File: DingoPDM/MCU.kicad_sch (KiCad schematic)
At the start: 25 parts, among them J4 TC, SW1 BOOT, U3 PCA82C250, U4 STM32F446RETx, Y1 8mHz

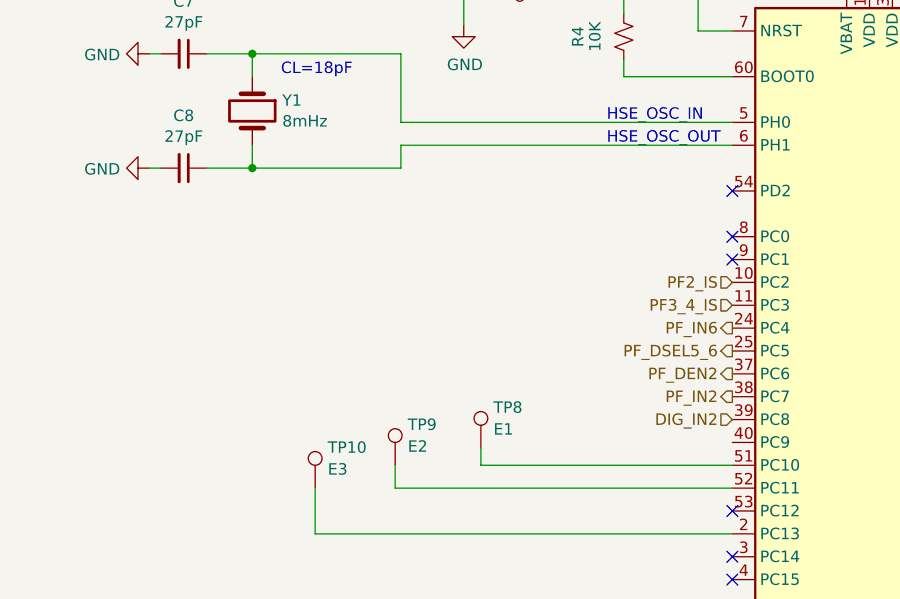
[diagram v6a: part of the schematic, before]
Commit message: V7.1 Fixes
SDA/SCL mixed up on FRAM, added status LEDs, switched to thermal relief zones
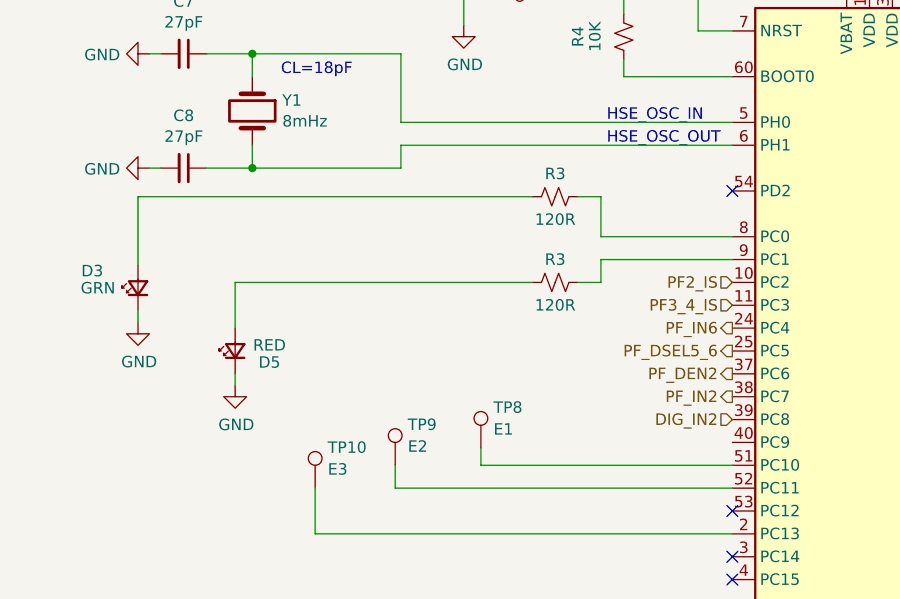
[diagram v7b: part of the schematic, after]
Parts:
- added D3: GRN, LED_SMD:LED_0805_2012Metric, symbol Device:LED_Small
- added D5: RED, LED_SMD:LED_0805_2012Metric, symbol Device:LED_Small
- added R3 (x2): 120R, Resistor_SMD:R_0805_2012Metric, symbol Device:R_Small_US
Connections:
- net GND: now also D3.1 (K), D5.1 (K)
- net at U4.8 (PC0): now also R3.1
- net at U4.9 (PC1): now also R3.1
- new net: D3.2 (A), R3.2
- new net: D5.2 (A), R3.2
- no-connect marks 9 -> 7
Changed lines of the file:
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@@
   (title_block
     (title "Dingo_PDM")
-    (date "2023-07-28")
-    (rev "v6")
+    (date "2023-09-04")
+    (rev "v7.1")
     (comment 3 "github.com/corygrant")
     (comment 4 "Cory Grant")
@@
   (junction (at 114.3 23.495) (diameter 0) (color 0 0 0 0)
   )
-  (no_connect (at 91.44 62.865))
   (no_connect (at 91.44 90.805))
   (no_connect (at 127 75.565))
   (no_connect (at 91.44 95.885))
   (no_connect (at 127 93.345))
-  (no_connect (at 91.44 60.325))
   (no_connect (at 127 90.805))
   (no_connect (at 91.44 98.425))
@@
     (stroke (width 0) (type default))
   )
+  (wire (pts (xy 69.215 55.88) (xy 25.4 55.88))
+    (stroke (width 0) (type default))
+  )
   (wire (pts (xy 114.3 23.495) (xy 114.3 32.385))
     (stroke (width 0) (type default))
@@
     (stroke (width 0) (type default))
   )
+  (wire (pts (xy 36.195 76.835) (xy 36.195 75.565))
+    (stroke (width 0) (type default))
+  )
   (wire (pts (xy 116.84 29.845) (xy 116.84 32.385))
     (stroke (width 0) (type default))
@@
     (stroke (width 0) (type default))
   )
+  (wire (pts (xy 76.835 60.325) (xy 76.835 55.88))
+    (stroke (width 0) (type default))
+  )
   (wire (pts (xy 79.375 167.64) (xy 85.725 167.64))
     (stroke (width 0) (type default))
@@
     (stroke (width 0) (type default))
   )
+  (wire (pts (xy 76.835 65.405) (xy 74.295 65.405))
+    (stroke (width 0) (type default))
+  )
+  (wire (pts (xy 76.835 62.865) (xy 76.835 65.405))
+    (stroke (width 0) (type default))
+  )
   (wire (pts (xy 98.425 184.15) (xy 98.425 180.34))
     (stroke (width 0) (type default))
@@
     (stroke (width 0) (type default))
   )
+  (wire (pts (xy 76.835 55.88) (xy 74.295 55.88))
+    (stroke (width 0) (type default))
+  )
   (wire (pts (xy 38.1 40.005) (xy 33.02 40.005))
     (stroke (width 0) (type default))
@@
     (stroke (width 0) (type default))
   )
+  (wire (pts (xy 25.4 55.88) (xy 25.4 63.5))
+    (stroke (width 0) (type default))
+  )
   (wire (pts (xy 63.5 85.725) (xy 63.5 83.82))
     (stroke (width 0) (type default))
@@
     (stroke (width 0) (type default))
   )
+  (wire (pts (xy 91.44 60.325) (xy 76.835 60.325))
+    (stroke (width 0) (type default))
+  )
   (wire (pts (xy 109.22 23.495) (xy 111.76 23.495))
     (stroke (width 0) (type default))
@@
     (stroke (width 0) (type default))
   )
+  (wire (pts (xy 25.4 69.85) (xy 25.4 68.58))
+    (stroke (width 0) (type default))
+  )
+  (wire (pts (xy 91.44 62.865) (xy 76.835 62.865))
+    (stroke (width 0) (type default))
+  )
   (wire (pts (xy 26.67 52.705) (xy 27.94 52.705))
     (stroke (width 0) (type default))
@@
     (stroke (width 0) (type default))
   )
+  (wire (pts (xy 69.215 65.405) (xy 36.195 65.405))
+    (stroke (width 0) (type default))
+  )
   (wire (pts (xy 38.1 50.165) (xy 38.1 52.705))
     (stroke (width 0) (type default))
@@
   )
   (wire (pts (xy 127 88.265) (xy 138.43 88.265))
+    (stroke (width 0) (type default))
+  )
+  (wire (pts (xy 36.195 65.405) (xy 36.195 70.485))
     (stroke (width 0) (type default))
   )
@@
     )
   )
+  (symbol (lib_id "Device:LED_Small") (at 25.4 66.04 90) (unit 1)
+    (in_bom yes) (on_board yes) (dnp no)
+    (property "Reference" "D3" (at 20.32 64.135 90)
+      (effects (font (size 1.27 1.27)))
+    )
+    (property "Value" "GRN" (at 20.955 66.04 90)
+      (effects (font (size 1.27 1.27)))
+    )
+    (property "Footprint" "LED_SMD:LED_0805_2012Metric" (at 25.4 66.04 90)
+      (effects (font (size 1.27 1.27)) hide)
+    )
+    (property "Datasheet" "" (at 25.4 66.04 90)
+      (effects (font (size 1.27 1.27)) hide)
+    )
+    (property "Digi-Key_PN" "475-1410-1-ND" (at 25.4 66.04 0)
+      (effects (font (size 1.27 1.27)) hide)
+    )
+    (property "LCSC" "C2899888" (at 25.4 66.04 0)
+      (effects (font (size 1.27 1.27)) hide)
+    )
+    (pin "1")
+    (pin "2")
+    (instances
+      (project "DingoPDM"
+        (path "/8948e307-9174-4227-9c28-3ff885e6e83d/00000000-0000-0000-0000-00005f5cf2eb"
+          (reference "D3") (unit 1)
+        )
+        (path "/8948e307-9174-4227-9c28-3ff885e6e83d/00000000-0000-0000-0000-00005f4db108"
+          (reference "D16") (unit 1)
+        )
+      )
+    )
+  )
   (symbol (lib_id "Connector:TestPoint") (at 64.135 151.13 180) (unit 1)
     (in_bom yes) (on_board yes) (dnp no)
@@
         (path "/8948e307-9174-4227-9c28-3ff885e6e83d/00000000-0000-0000-0000-00005f4db108"
           (reference "TP2") (unit 1)
+        )
+      )
+    )
+  )
+  (symbol (lib_id "power:GND") (at 36.195 76.835 0) (unit 1)
+    (in_bom yes) (on_board yes) (dnp no)
+    (property "Reference" "#PWR016" (at 36.195 83.185 0)
+      (effects (font (size 1.27 1.27)) hide)
+    )
+    (property "Value" "GND" (at 36.322 81.2292 0)
+      (effects (font (size 1.27 1.27)))
+    )
+    (property "Footprint" "" (at 36.195 76.835 0)
+      (effects (font (size 1.27 1.27)) hide)
+    )
+    (property "Datasheet" "" (at 36.195 76.835 0)
+      (effects (font (size 1.27 1.27)) hide)
+    )
+    (pin "1")
+    (instances
+      (project "DingoPDM"
+        (path "/8948e307-9174-4227-9c28-3ff885e6e83d/00000000-0000-0000-0000-00005f5cf2eb"
+          (reference "#PWR016") (unit 1)
+        )
+        (path "/8948e307-9174-4227-9c28-3ff885e6e83d/00000000-0000-0000-0000-00005f4db108"
+          (reference "#PWR091") (unit 1)
         )
       )
@@
     )
   )
+  (symbol (lib_id "Device:R_Small_US") (at 71.755 65.405 270) (unit 1)
+    (in_bom yes) (on_board yes) (dnp no)
+    (property "Reference" "R3" (at 71.755 62.865 90)
+      (effects (font (size 1.27 1.27)))
+    )
+    (property "Value" "120R" (at 71.755 67.945 90)
+      (effects (font (size 1.27 1.27)))
+    )
+    (property "Footprint" "Resistor_SMD:R_0805_2012Metric" (at 71.755 65.405 0)
+      (effects (font (size 1.27 1.27)) hide)
+    )
+    (property "Datasheet" "" (at 71.755 65.405 0)
+      (effects (font (size 1.27 1.27)) hide)
+    )
+    (property "Digi-Key_PN" "311-120CRCT-ND" (at 71.755 65.405 0)
+      (effects (font (size 1.27 1.27)) hide)
+    )
+    (property "LCSC" "C229076" (at 71.755 65.405 0)
+      (effects (font (size 1.27 1.27)) hide)
+    )
+    (pin "1")
+    (pin "2")
+    (instances
+      (project "DingoPDM"
+        (path "/8948e307-9174-4227-9c28-3ff885e6e83d/00000000-0000-0000-0000-00005f5cf2eb"
+          (reference "R3") (unit 1)
+        )
+        (path "/8948e307-9174-4227-9c28-3ff885e6e83d/00000000-0000-0000-0000-00005f4db108"
+          (reference "R53") (unit 1)
+        )
+      )
+    )
+  )
   (symbol (lib_id "Connector:TestPoint") (at 45.085 88.265 0) (unit 1)
     (in_bom yes) (on_board yes) (dnp no) (fields_autoplaced)
@@
     )
   )
+  (symbol (lib_id "Device:LED_Small") (at 36.195 73.025 90) (unit 1)
+    (in_bom yes) (on_board yes) (dnp no)
+    (property "Reference" "D5" (at 40.005 74.295 90)
+      (effects (font (size 1.27 1.27)))
+    )
+    (property "Value" "RED" (at 40.005 72.39 90)
+      (effects (font (size 1.27 1.27)))
+    )
+    (property "Footprint" "LED_SMD:LED_0805_2012Metric" (at 36.195 73.025 90)
+      (effects (font (size 1.27 1.27)) hide)
+    )
+    (property "Datasheet" "" (at 36.195 73.025 90)
+      (effects (font (size 1.27 1.27)) hide)
+    )
+    (property "Digi-Key_PN" "475-1278-1-ND" (at 36.195 73.025 0)
+      (effects (font (size 1.27 1.27)) hide)
+    )
+    (property "LCSC" "C2899997" (at 36.195 73.025 0)
+      (effects (font (size 1.27 1.27)) hide)
+    )
+    (pin "1")
+    (pin "2")
+    (instances
+      (project "DingoPDM"
+        (path "/8948e307-9174-4227-9c28-3ff885e6e83d/00000000-0000-0000-0000-00005f5b7065"
+          (reference "D5") (unit 1)
+        )
+        (path "/8948e307-9174-4227-9c28-3ff885e6e83d/00000000-0000-0000-0000-00005f4db108"
+          (reference "D17") (unit 1)
+        )
+      )
+    )
+  )
+  (symbol (lib_id "power:GND") (at 25.4 69.85 0) (unit 1)
+    (in_bom yes) (on_board yes) (dnp no)
+    (property "Reference" "#PWR016" (at 25.4 76.2 0)
+      (effects (font (size 1.27 1.27)) hide)
+    )
+    (property "Value" "GND" (at 25.527 74.2442 0)
+      (effects (font (size 1.27 1.27)))
+    )
+    (property "Footprint" "" (at 25.4 69.85 0)
+      (effects (font (size 1.27 1.27)) hide)
+    )
+    (property "Datasheet" "" (at 25.4 69.85 0)
+      (effects (font (size 1.27 1.27)) hide)
+    )
+    (pin "1")
+    (instances
+      (project "DingoPDM"
+        (path "/8948e307-9174-4227-9c28-3ff885e6e83d/00000000-0000-0000-0000-00005f5cf2eb"
+          (reference "#PWR016") (unit 1)
+        )
+        (path "/8948e307-9174-4227-9c28-3ff885e6e83d/00000000-0000-0000-0000-00005f4db108"
+          (reference "#PWR090") (unit 1)
+        )
+      )
+    )
+  )
   (symbol (lib_id "Connector:TestPoint") (at 70.485 151.13 180) (unit 1)
     (in_bom yes) (on_board yes) (dnp no)
@@
         )
       )
+    )
+  )
+  (symbol (lib_id "Device:R_Small_US") (at 71.755 55.88 270) (unit 1)
+    (in_bom yes) (on_board yes) (dnp no)
+    (property "Reference" "R3" (at 71.755 53.34 90)
+      (effects (font (size 1.27 1.27)))
+    )
+    (property "Value" "120R" (at 71.755 58.42 90)
+      (effects (font (size 1.27 1.27)))
+    )
+    (property "Footprint" "Resistor_SMD:R_0805_2012Metric" (at 71.755 55.88 0)
+      (effects (font (size 1.27 1.27)) hide)
+    )
+    (property "Datasheet" "" (at 71.755 55.88 0)
+      (effects (font (size 1.27 1.27)) hide)
+    )
+    (property "Digi-Key_PN" "311-120CRCT-ND" (at 71.755 55.88 0)
+      (effects (font (size 1.27 1.27)) hide)
+    )
+    (property "LCSC" "C229076" (at 71.755 55.88 0)
+      (effects (font (size 1.27 1.27)) hide)
+    )
+    (pin "1")
+    (pin "2")
+    (instances
+      (project "DingoPDM"
+        (path "/8948e307-9174-4227-9c28-3ff885e6e83d/00000000-0000-0000-0000-00005f5cf2eb"
+          (reference "R3") (unit 1)
+        )
+        (path "/8948e307-9174-4227-9c28-3ff885e6e83d/00000000-0000-0000-0000-00005f4db108"
+          (reference "R52") (unit 1)
+        )
+      )

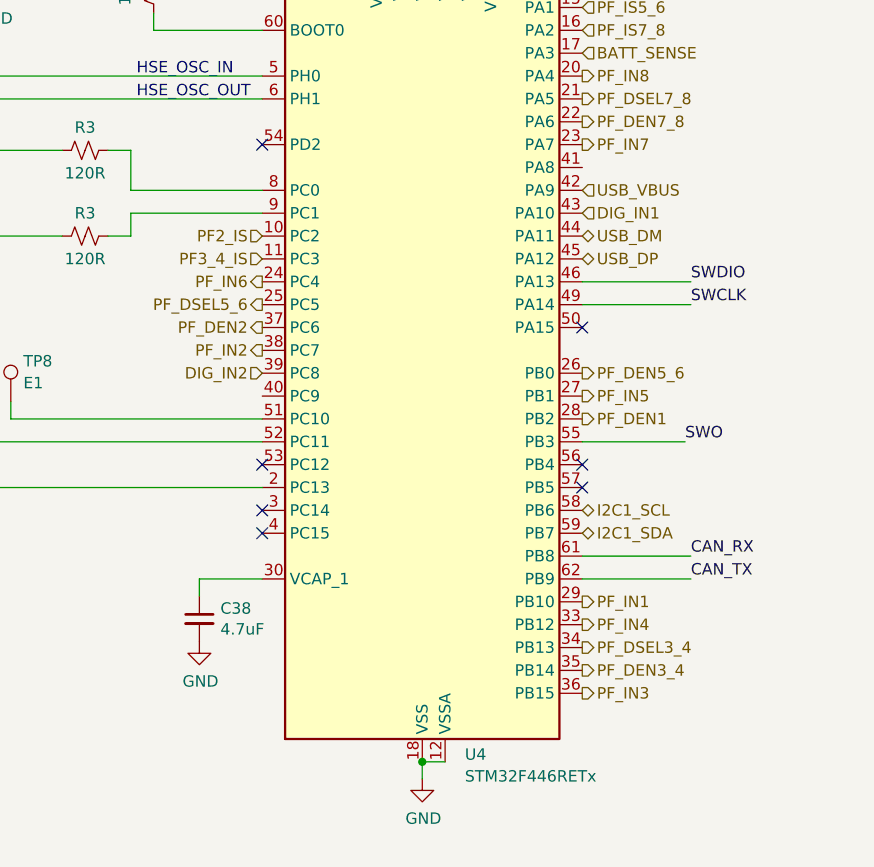
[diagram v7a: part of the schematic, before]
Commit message: Add diode, disconnect PB13, fix USB VBUS
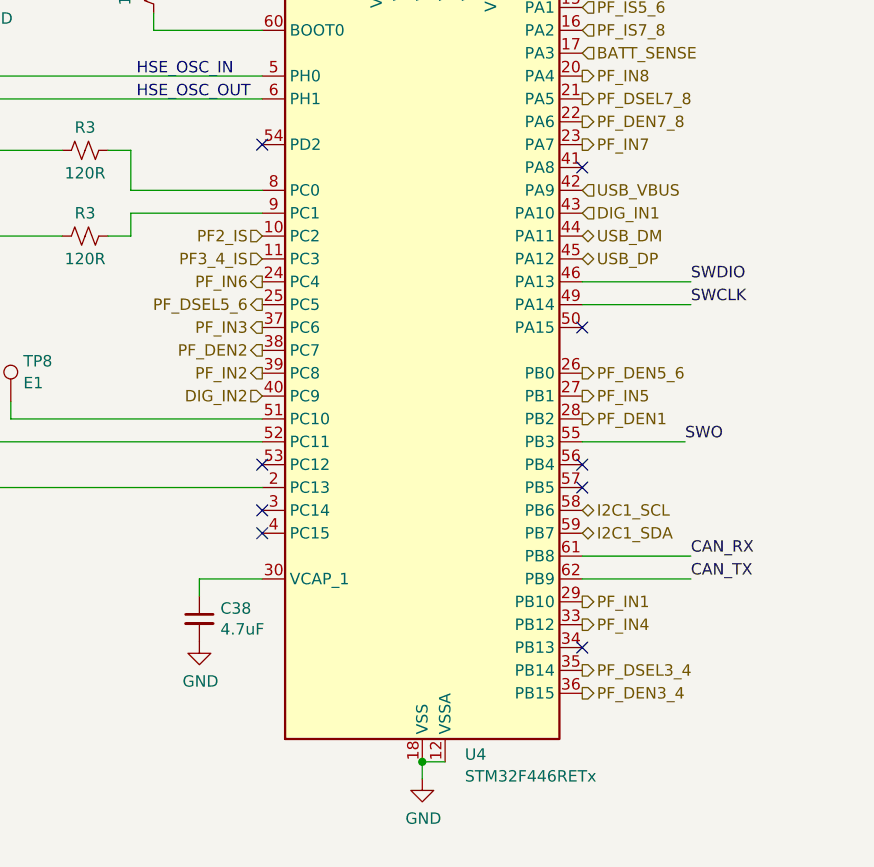
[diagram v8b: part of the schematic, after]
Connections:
- net DIG_IN2: now also U4.40 (PC9); no longer U4.39 (PC8)
- net PF_DEN2: now also U4.38 (PC7); no longer U4.37 (PC6)
- net PF_DEN3_4: now also U4.36 (PB15); no longer U4.35 (PB14)
- net PF_DSEL3_4: now also U4.35 (PB14); no longer U4.34 (PB13)
- net PF_IN2: now also U4.39 (PC8); no longer U4.38 (PC7)
- net PF_IN3: now also U4.37 (PC6); no longer U4.36 (PB15)
- no-connect marks 7 -> 9
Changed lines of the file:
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@@
   (title_block
     (title "Dingo_PDM")
-    (date "2023-09-04")
-    (rev "v7.1")
+    (date "2023-09-11")
+    (rev "v7.2")
     (comment 3 "github.com/corygrant")
     (comment 4 "Cory Grant")
@@
   (junction (at 114.3 23.495) (diameter 0) (color 0 0 0 0)
   )
+  (no_connect (at 127 111.125))
+  (no_connect (at 127 57.785))
   (no_connect (at 91.44 90.805))
   (no_connect (at 127 75.565))
@@
     (effects (font (size 1.27 1.27)) (justify left))
   )
-  (hierarchical_label "PF_IN2" (shape output) (at 91.44 78.105 180) (fields_autoplaced)
+  (hierarchical_label "PF_IN2" (shape output) (at 91.44 80.645 180) (fields_autoplaced)
     (effects (font (size 1.27 1.27)) (justify right))
   )
@@
     (effects (font (size 1.27 1.27)) (justify left))
   )
-  (hierarchical_label "DIG_IN2" (shape input) (at 91.44 80.645 180) (fields_autoplaced)
+  (hierarchical_label "DIG_IN2" (shape input) (at 91.44 83.185 180) (fields_autoplaced)
     (effects (font (size 1.27 1.27)) (justify right))
   )
-  (hierarchical_label "PF_DSEL3_4" (shape output) (at 127 111.125 0) (fields_autoplaced)
+  (hierarchical_label "PF_DSEL3_4" (shape output) (at 127 113.665 0) (fields_autoplaced)
     (effects (font (size 1.27 1.27)) (justify left))
   )
@@
     (effects (font (size 1.27 1.27)) (justify right))
   )
-  (hierarchical_label "PF_DEN2" (shape output) (at 91.44 75.565 180) (fields_autoplaced)
+  (hierarchical_label "PF_DEN2" (shape output) (at 91.44 78.105 180) (fields_autoplaced)
     (effects (font (size 1.27 1.27)) (justify right))
   )
-  (hierarchical_label "PF_IN3" (shape output) (at 127 116.205 0) (fields_autoplaced)
-    (effects (font (size 1.27 1.27)) (justify left))
+  (hierarchical_label "PF_IN3" (shape output) (at 91.44 75.565 180) (fields_autoplaced)
+    (effects (font (size 1.27 1.27)) (justify right))
   )
   (hierarchical_label "PF_IN4" (shape output) (at 127 108.585 0) (fields_autoplaced)
@@
     (effects (font (size 1.27 1.27)) (justify left))
   )
-  (hierarchical_label "PF_DEN3_4" (shape output) (at 127 113.665 0) (fields_autoplaced)
-    (effects (font (size 1.27 1.27)) (justify left))
-  )
+  (hierarchical_label "PF_DEN3_4" (shape output) (at 127 116.205 0) (fields_autoplaced)
+    (effects (font (size 1.27 1.27)) (justify left))
+  )
